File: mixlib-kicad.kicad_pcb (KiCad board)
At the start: 2 copper layers, 0 parts

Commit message: feat: add a bunch of new components
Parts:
- added REF**: TSOP-6_1.65x3.05mm_P0.95mm, Package_SO:TSOP-6_1.65x3.05mm_P0.95mm, F.Cu at (150.6, 74.2)
- added REF**: TSOT-23-6_HandSoldering, Package_TO_SOT_SMD:TSOT-23-6_HandSoldering, F.Cu at (157.0, 73.7)

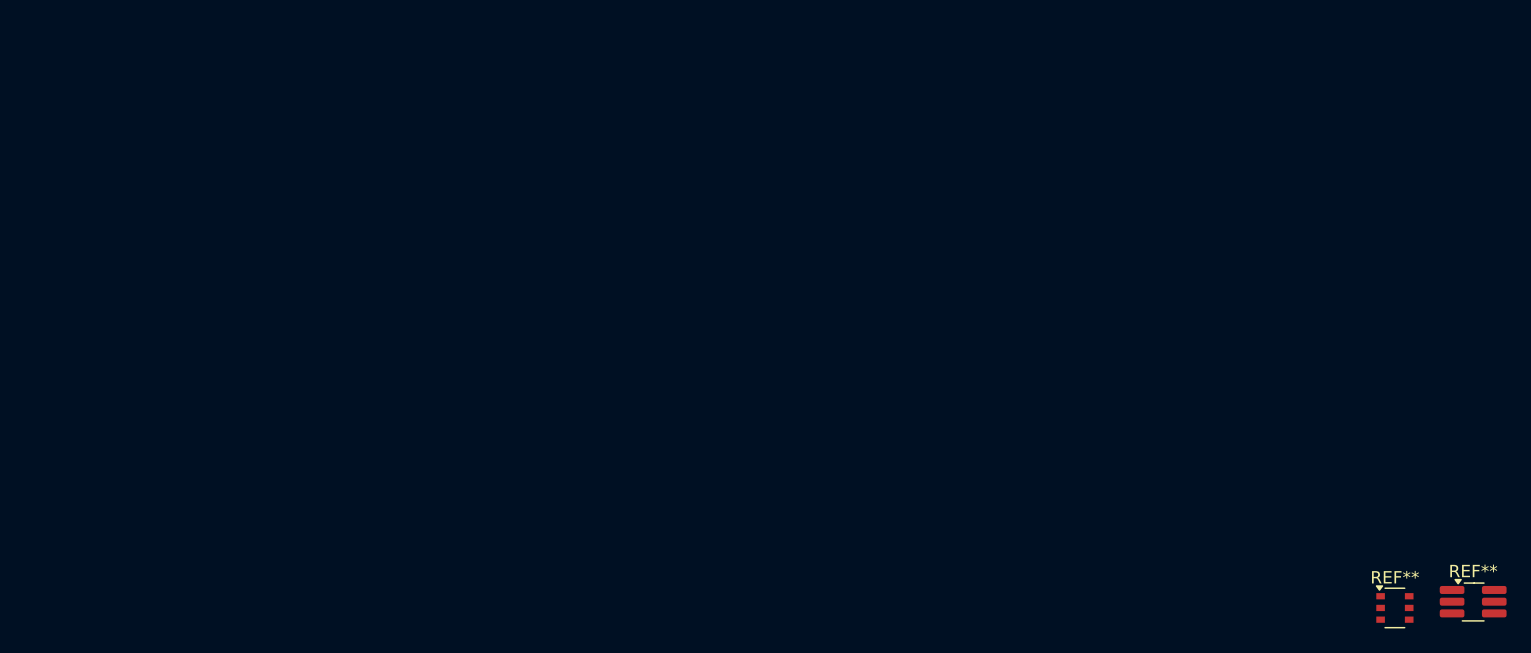
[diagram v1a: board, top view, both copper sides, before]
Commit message: fix(pmic-battery): bq25672: minor adjustments to the footprint
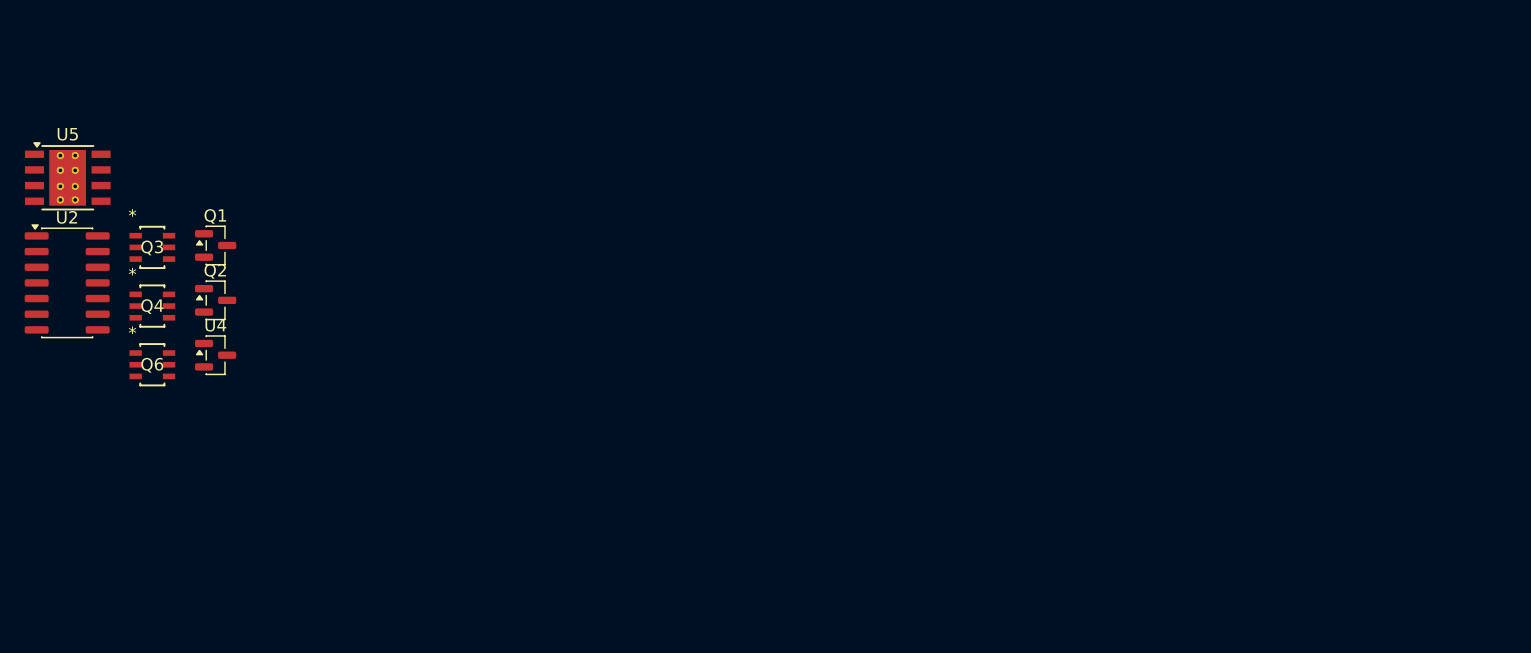
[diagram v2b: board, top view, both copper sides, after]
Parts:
- removed REF**: TSOP-6_1.65x3.05mm_P0.95mm, Package_SO:TSOP-6_1.65x3.05mm_P0.95mm
- removed REF**: TSOT-23-6_HandSoldering, Package_TO_SOT_SMD:TSOT-23-6_HandSoldering
- added Q1: MMBT5551L, Package_TO_SOT_SMD:SOT-23, F.Cu at (55.0, 44.8)
- added Q2: MMBT5551L, Package_TO_SOT_SMD:SOT-23, F.Cu at (55.0, 49.2)
- added Q3: PMD3001D, mixlib-generic-sot:SC-74_SOT-457_NEX, F.Cu at (49.8, 44.9)
- added Q4: PBSS4160DS, mixlib-generic-sot:SC-74_SOT-457_NEX, F.Cu at (49.8, 49.7)
- added Q6: PBSS4160DPN, mixlib-generic-sot:SC-74_SOT-457_NEX, F.Cu at (49.8, 54.4)
- added U2: MCP6404, Package_SO:SOIC-14_3.9x8.7mm_P1.27mm, F.Cu at (42.9, 47.8)
- added U4: LM4040DBZ-10, Package_TO_SOT_SMD:SOT-23, F.Cu at (55.0, 53.7)
- added U5: TPS5430DDA, Package_SO:TI_SO-PowerPAD-8_ThermalVias, F.Cu at (43.0, 39.3)

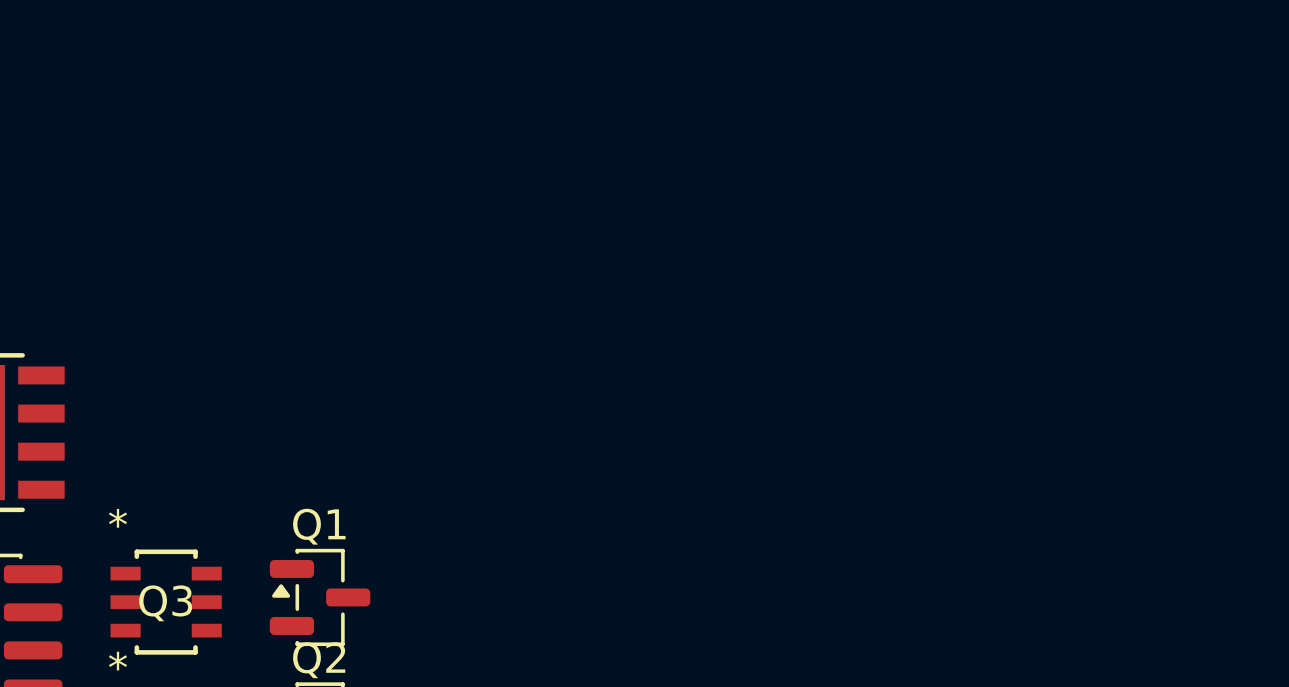
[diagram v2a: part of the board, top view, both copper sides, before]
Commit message: feat(discrete-mosfet): add DMN31D5UDJ
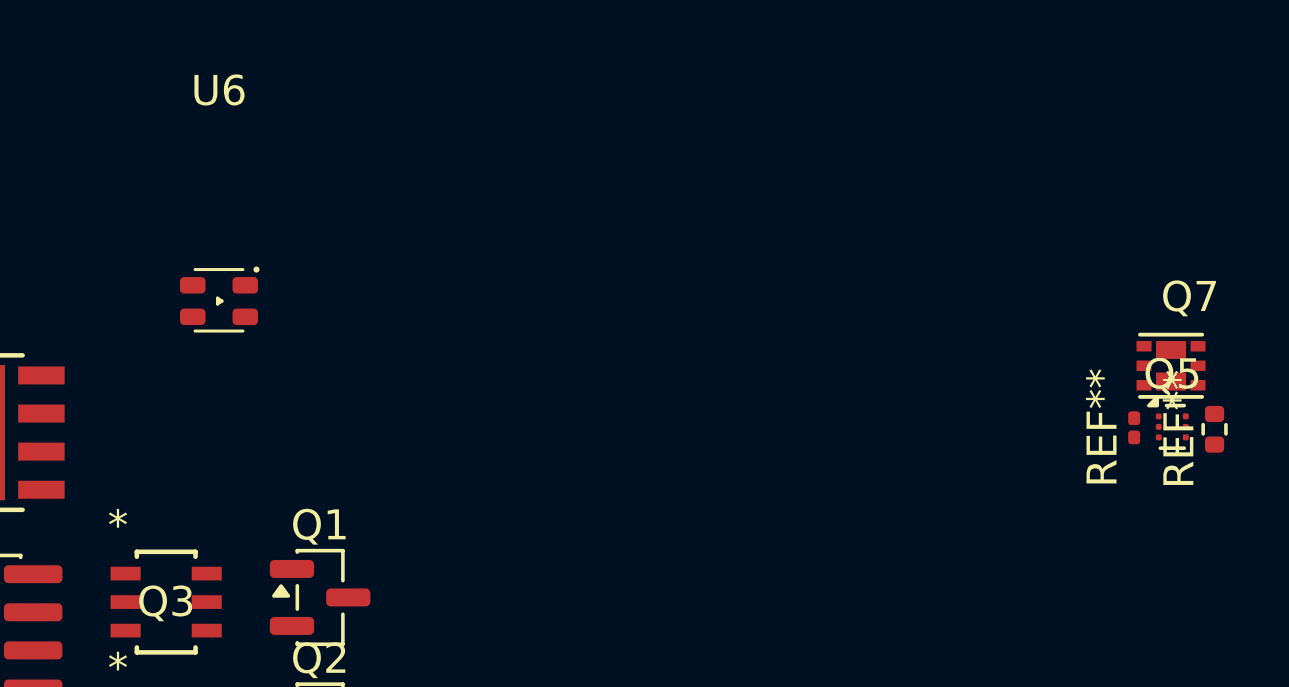
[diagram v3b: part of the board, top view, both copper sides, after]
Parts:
- added Q5: DMC2990UDJQ, mixlib-generic-sot:SOT-963, F.Cu at (83.4, 39.1)
- added Q7: DMN3032LFDBQ, mixlib-generic-dfn:Diodes-Incorporated_U-DFN2020-6_Type-B, F.Cu at (83.3, 37.0)
- added REF**: R_0402_1005Metric, Resistor_SMD:R_0402_1005Metric, F.Cu at (84.8, 39.2)
- added REF**: R_0201_0603Metric, Resistor_SMD:R_0201_0603Metric, F.Cu at (82.1, 39.1)
- added U6: TJ-S1615CY6TGLCCYRGY-A5, mixlib-discrete-led:LED-3_RGB-0603_1615Metric, F.Cu at (51.6, 34.9)
